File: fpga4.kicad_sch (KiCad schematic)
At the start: 11 parts, among them P1 5CEFA7F23

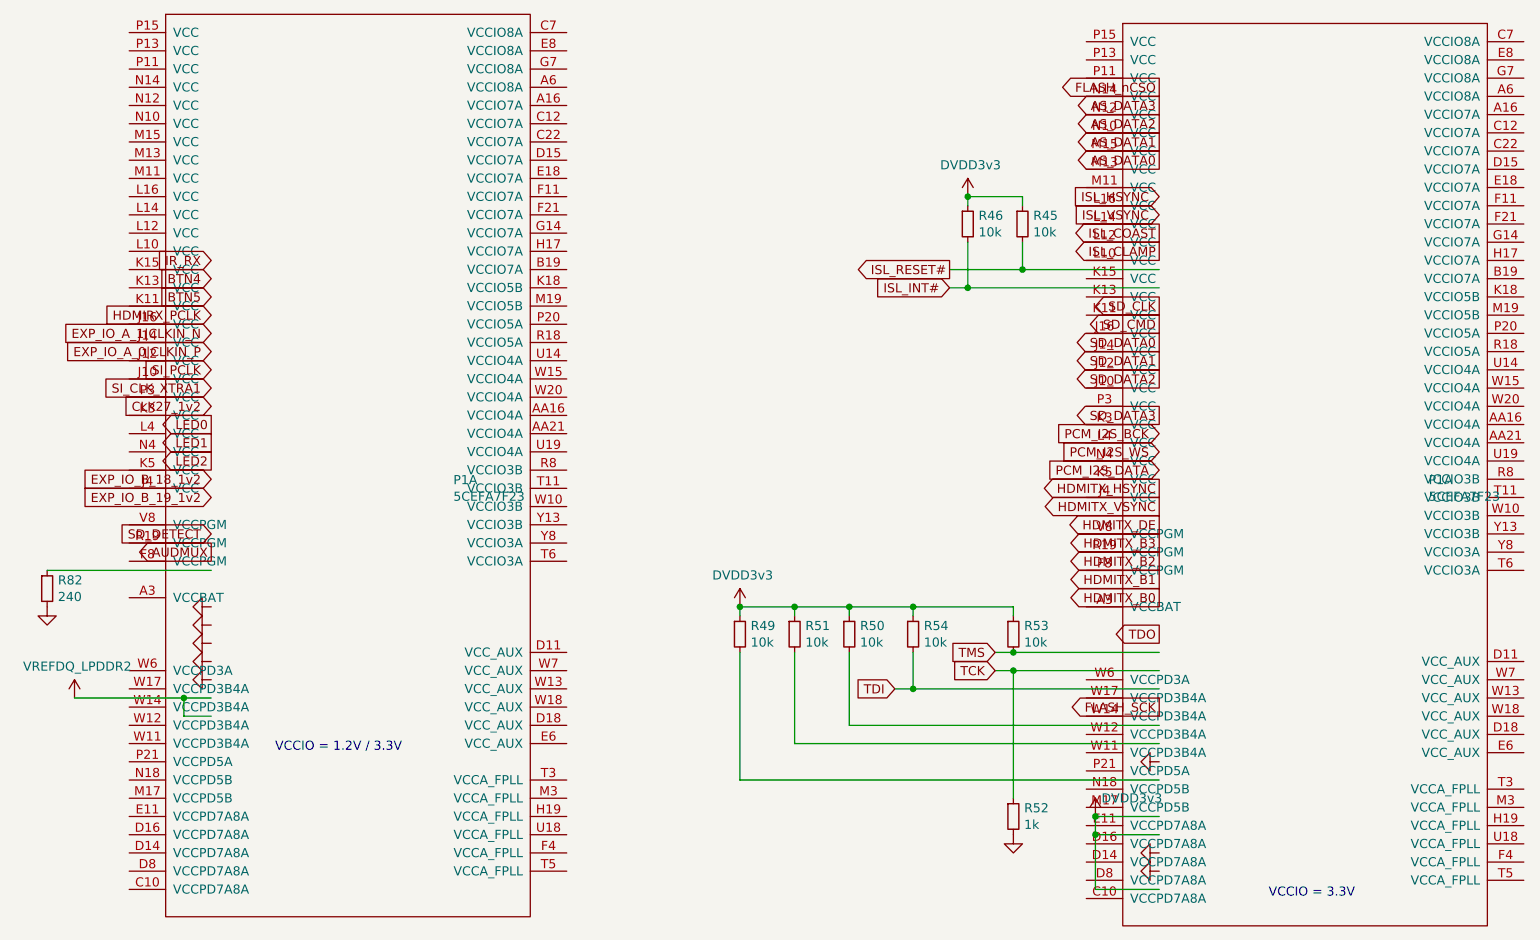
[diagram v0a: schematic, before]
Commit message: update schematic to v1.5
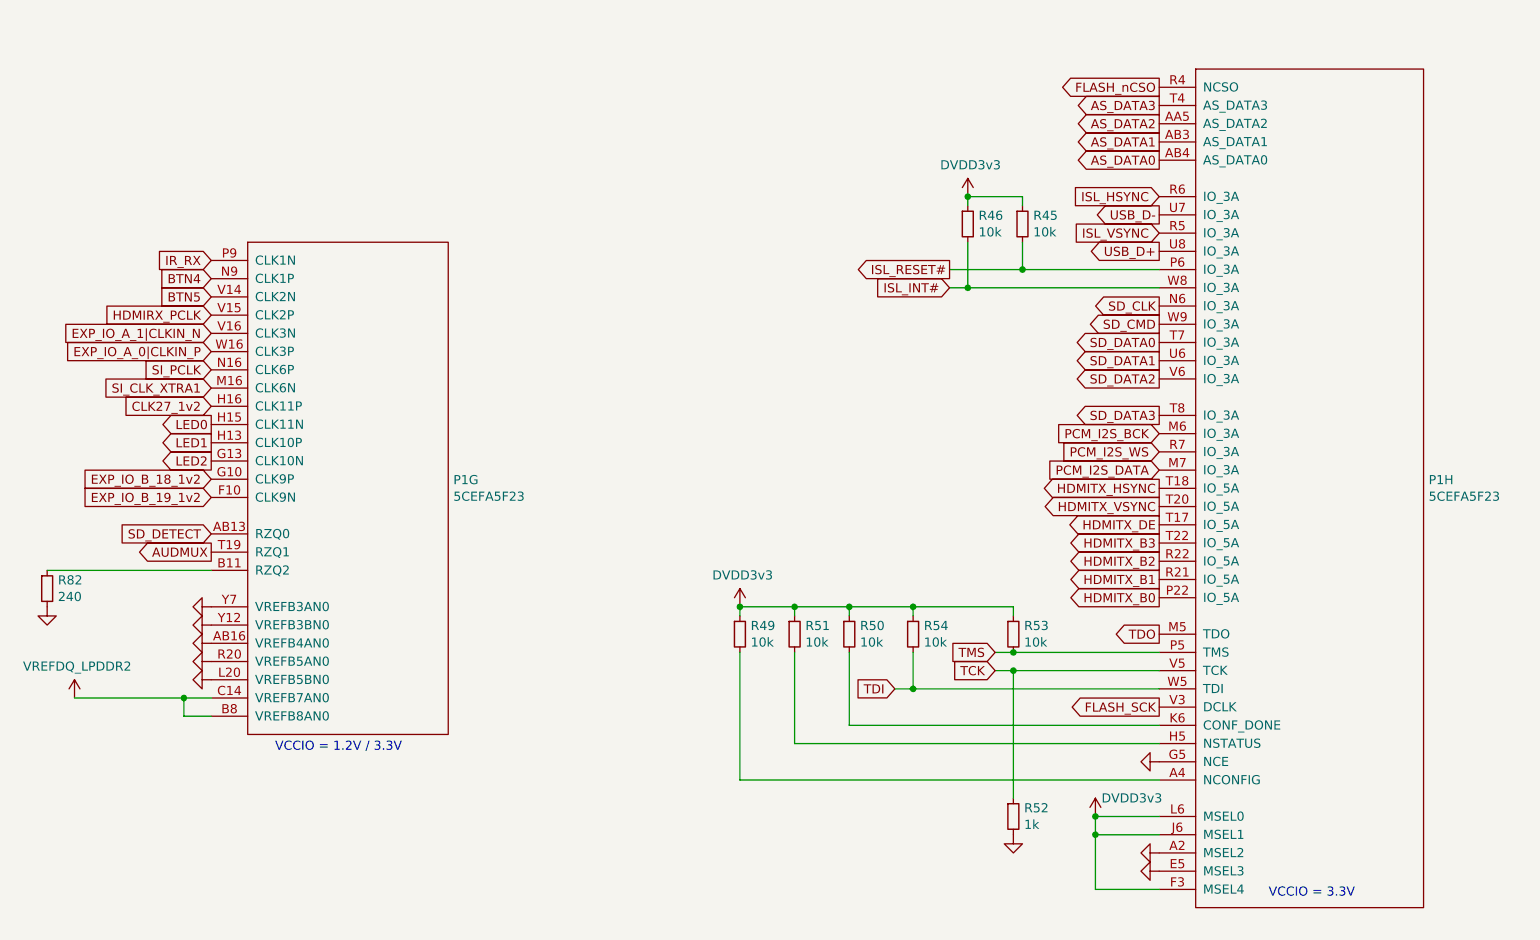
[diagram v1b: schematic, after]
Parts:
- P1: value 5CEFA7F23 -> 5CEFA5F23
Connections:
- net AS_DATA0: now also P1.AB4 (AS_DATA0)
- net AS_DATA1: now also P1.AB3 (AS_DATA1)
- net AS_DATA2: now also P1.AA5 (AS_DATA2)
- net AS_DATA3: now also P1.T4 (AS_DATA3)
- net AUDMUX: now also P1.T19 (RZQ1)
- net BTN4: now also P1.N9 (CLK1P)
- net BTN5: now also P1.V14 (CLK2N)
- net CLK27_1v2: now also P1.H16 (CLK11P)
- net DVDD3v3: now also P1.F3 (MSEL4), P1.J6 (MSEL1), P1.L6 (MSEL0)
- net EXP_IO_A_0|CLKIN_P: now also P1.W16 (CLK3P)
- net EXP_IO_A_1|CLKIN_N: now also P1.V16 (CLK3N)
- net EXP_IO_B_18_1v2: now also P1.G10 (CLK9P)
- net EXP_IO_B_19_1v2: now also P1.F10 (CLK9N)
- net FLASH_SCK: now also P1.V3 (DCLK)
- net FLASH_nCSO: now also P1.R4 (NCSO)
- net GND: now also P1.A2 (MSEL2), P1.AB16 (VREFB4AN0), P1.E5 (MSEL3), P1.G5 (NCE), P1.L20 (VREFB5BN0), P1.R20 (VREFB5AN0), P1.Y12 (VREFB3BN0), P1.Y7 (VREFB3AN0)
- net HDMIRX_PCLK: now also P1.V15 (CLK2P)
- net HDMITX_B0: now also P1.P22 (IO_5A)
- net HDMITX_B1: now also P1.R21 (IO_5A)
- net HDMITX_B2: now also P1.R22 (IO_5A)
- net HDMITX_B3: now also P1.T22 (IO_5A)
- net HDMITX_DE: now also P1.T17 (IO_5A)
- net HDMITX_HSYNC: now also P1.T18 (IO_5A)
- net HDMITX_VSYNC: now also P1.T20 (IO_5A)
- net IR_RX: now also P1.P9 (CLK1N)
- net ISL_HSYNC: now also P1.R6 (IO_3A)
- net ISL_INT#: now also P1.W8 (IO_3A)
- net ISL_RESET#: now also P1.P6 (IO_3A)
- net ISL_VSYNC: now also P1.R5 (IO_3A)
- net LED0: now also P1.H15 (CLK11N)
- net LED1: now also P1.H13 (CLK10P)
- net LED2: now also P1.G13 (CLK10N)
- net PCM_I2S_BCK: now also P1.M6 (IO_3A)
- net PCM_I2S_DATA: now also P1.M7 (IO_3A)
- net PCM_I2S_WS: now also P1.R7 (IO_3A)
- net SD_CLK: now also P1.N6 (IO_3A)
- net SD_CMD: now also P1.W9 (IO_3A)
- net SD_DATA0: now also P1.T7 (IO_3A)
- net SD_DATA1: now also P1.U6 (IO_3A)
- net SD_DATA2: now also P1.V6 (IO_3A)
- net SD_DATA3: now also P1.T8 (IO_3A)
- net SD_DETECT: now also P1.AB13 (RZQ0)
- net SI_CLK_XTRA1: now also P1.M16 (CLK6N)
- net SI_PCLK: now also P1.N16 (CLK6P)
- net TCK: now also P1.V5 (TCK)
- net TDI: now also P1.W5 (TDI)
- net TDO: now also P1.M5 (TDO)
- net TMS: now also P1.P5 (TMS)
- net VREFDQ_LPDDR2: now also P1.B8 (VREFB8AN0), P1.C14 (VREFB7AN0)
- net at R82.1: now also P1.B11 (RZQ2)
- net at R50.2: now also P1.K6 (CONF_DONE)
- net at R51.2: now also P1.H5 (NSTATUS)
- net at R49.2: now also P1.A4 (NCONFIG)
- new net USB_D+: P1.U8 (IO_3A)
- new net USB_D-: P1.U7 (IO_3A)
